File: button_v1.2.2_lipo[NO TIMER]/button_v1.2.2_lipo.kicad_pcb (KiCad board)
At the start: 2 copper layers, 21 x 41.7 mm, 17 parts, among them J1 Conn_01x05_Female, SW1 SW_Push, SW2 SW_Push, U2 AP2112K-3.3, X1 ESP-12E

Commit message: 23.02 00:38
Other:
- board text added: "LK"

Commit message: :rocket: :full_moon_with_face:
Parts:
- moved D1 0.34 mm to (119.0, 62.7), turned to 0 degrees
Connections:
- D1 pad 1: /GND -> Net-(D1-Pad1)
- D1 pad 2: Net-(D1-Pad2) -> /VCC
- R6 pad 1: Net-(D1-Pad2) -> Net-(D1-Pad1)
- R6 pad 2: Net-(R6-Pad2) -> /RST
- SW1 pad 1: Net-(R6-Pad2) -> /RST
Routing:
- net /GND: track 90.2 -> 73.2 mm
- net /RST: track 40.0 -> 54.3 mm
- net /VCC: track 42.2 -> 53.5 mm
- net Net-(R6-Pad2): track 9.45 -> 0.00 mm
- net Net-(D1-Pad2): vias 1 -> 0
- net Net-(D1-Pad1): vias 0 -> 1

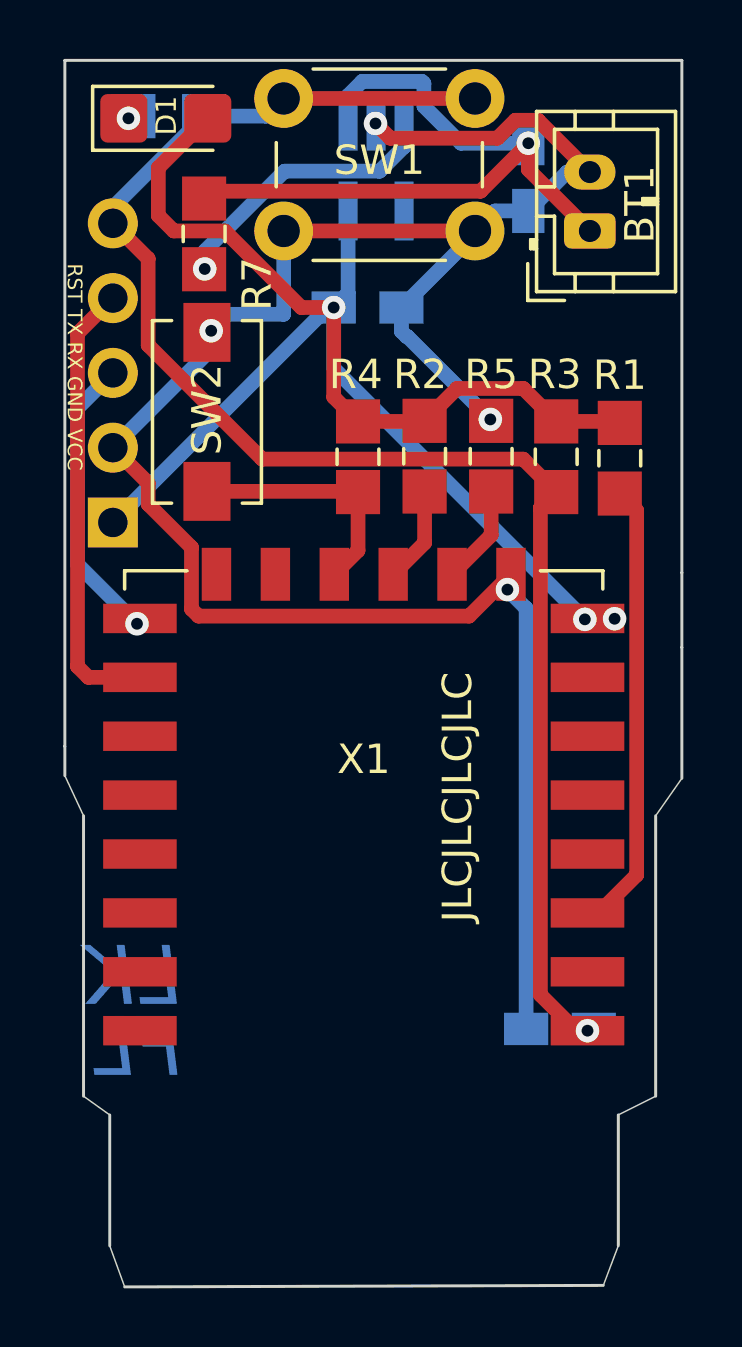
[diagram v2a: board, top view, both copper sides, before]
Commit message: 3D Models etwas verbessert
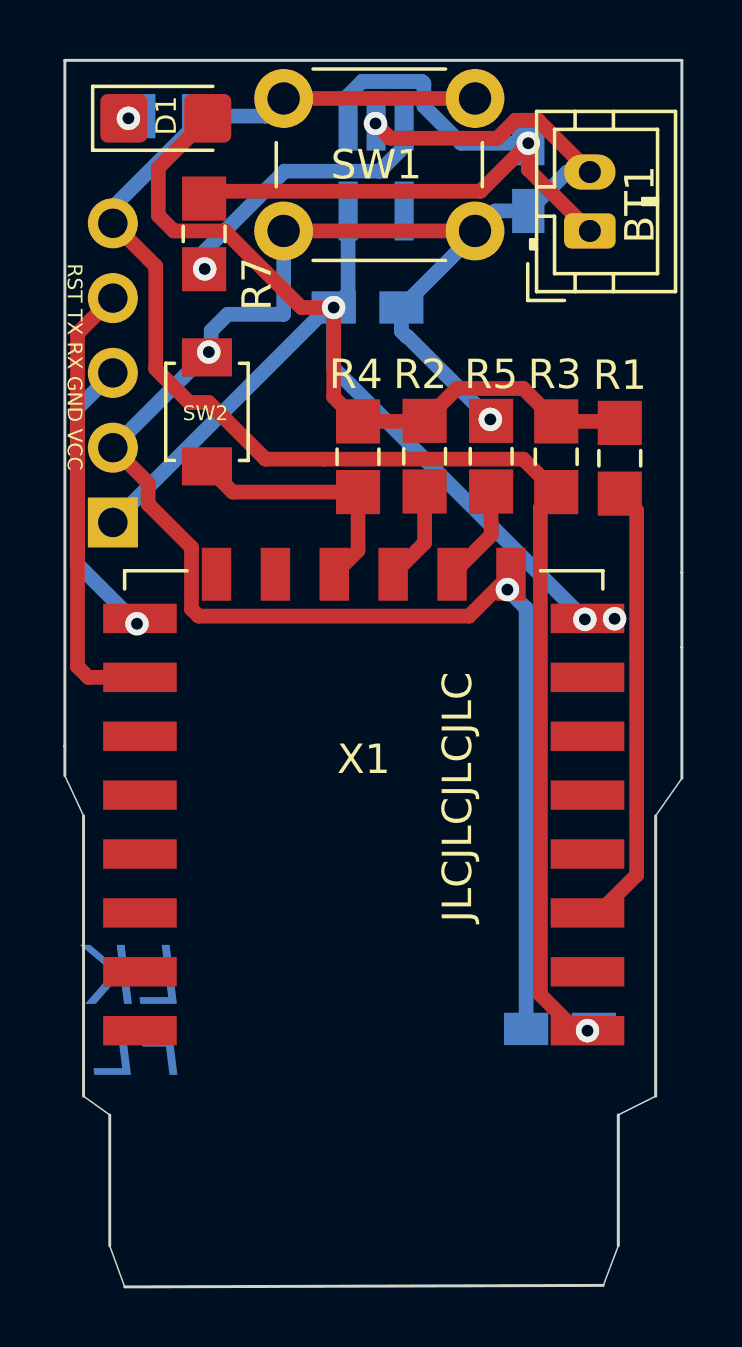
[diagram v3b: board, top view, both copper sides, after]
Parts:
- J1: footprint Connector_PinHeader_2.54mm:PinHeader_1x05_P2.54mm_Vertical -> handsolder:PinSocket_1x05_P2.54mm_Vertical_mod
- SW1: footprint Button_Switch_THT:SW_PUSH_6mm -> handsolder:SW_PUSH_6mm_H8mm_mod
- SW2: footprint Button_Switch_SMD:SW_SPST_EVQPE1 -> handsolder:SW_SPST_B3U-1000P_mod

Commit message: :rocket:  :new_moon:
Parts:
- moved R1 0.15 mm to (134.6, 74.2)

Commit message: cap between esp vcc and ground added
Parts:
- added C4: TAJB476M010TNJ, SamacSys_Parts:CAPPM3528X210N, B.Cu at (133.4, 81.0)
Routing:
- net /GND: track 73.2 -> 85.2 mm

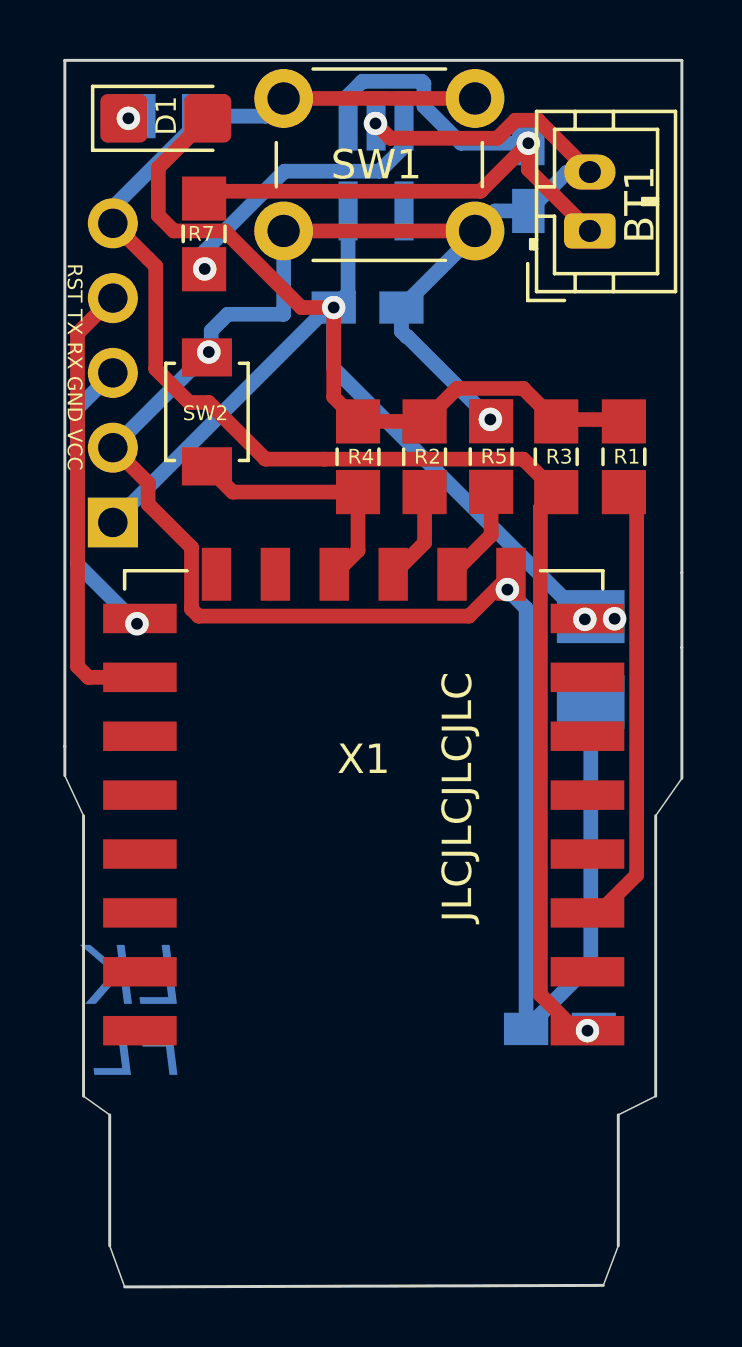
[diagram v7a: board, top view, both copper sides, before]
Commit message: Added 100nF decoupling capacitors between VCC and Ground of the ESP
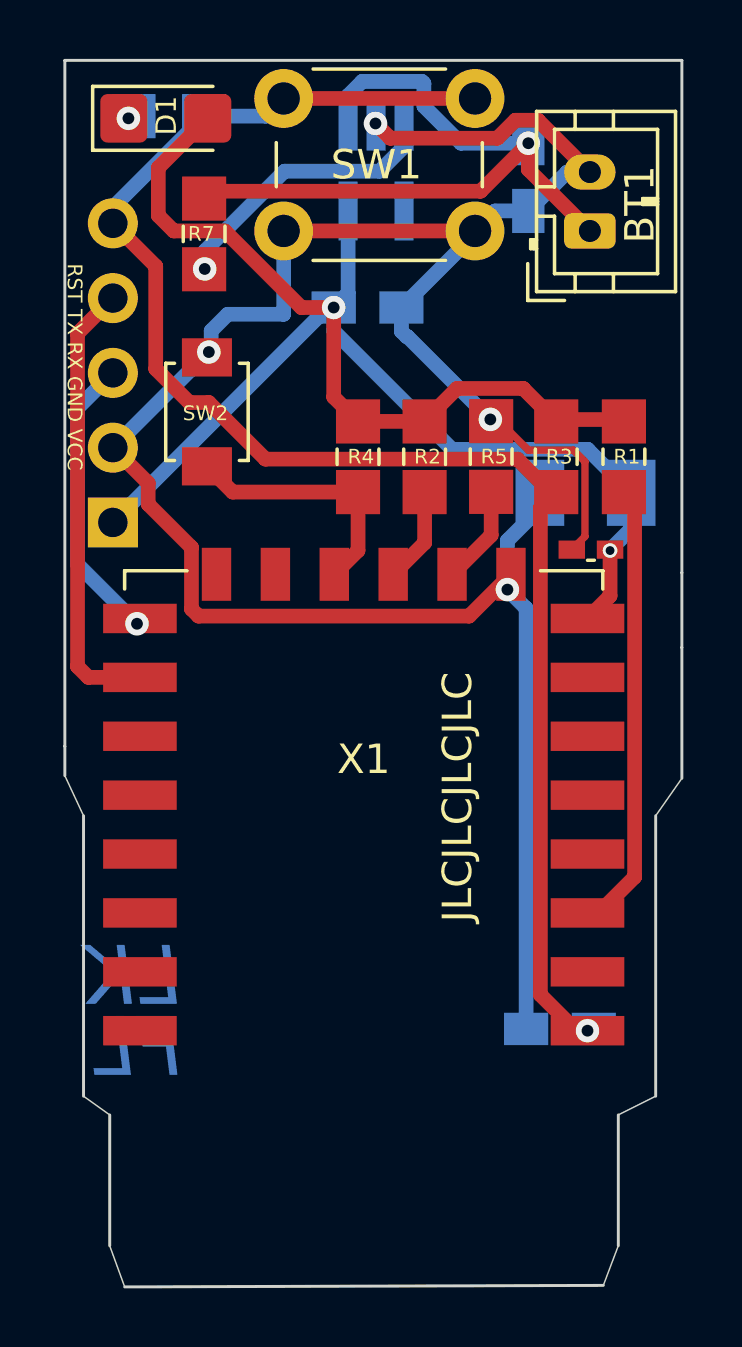
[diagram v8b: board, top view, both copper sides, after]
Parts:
- added C5: 100nF, handsolder:C_0402_1005Metric_Pad0.74x0.62mm_HandSoldermod, F.Cu at (133.4, 77.3)
- moved C4 5.66 mm to (133.3, 75.4), turned to 180 degrees
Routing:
- net /VCC: track 53.5 -> 57.3 mm, vias 3 -> 2
- net /GND: track 85.2 -> 83.9 mm
